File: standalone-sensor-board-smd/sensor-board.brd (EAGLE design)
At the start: 11 x 93.5 mm, 15 parts, among them Q1 QRE1113, Q2 QRE1113, Q3 QRE1113, Q4 QRE1113, Q5 QRE1113, Q6 QRE1113, Q7 QRE1113

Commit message: init smd
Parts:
- Q1, Q2, Q3, Q4, Q5, Q6, Q7: value QRE1113 -> QRE1113GR; device qre1113:DIP4_100AQ_ONS -> qre1113:DIP4_100AQ_ONS_SMD
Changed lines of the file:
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@@
 </autorouter>
 <elements>
-<element name="Q1" library="qre1113" package="DIP4_100AQ_ONS" value="QRE1113" x="1.705" y="3.71" smashed="yes">
+<element name="Q1" library="qre1113" package="DIP4_100AQ_ONS_SMD" value="QRE1113GR" x="1.705" y="3.71" smashed="yes">
 <attribute name="COPYRIGHT" value="Copyright (C) 2024 Ultra Librarian. All rights reserved." x="60.125" y="-8.99" size="1.778" layer="27" display="off"/>
 <attribute name="MANUFACTURER_PART_NUMBER" value="QRE1113" x="60.125" y="-8.99" size="1.778" layer="27" display="off"/>
@@
 <attribute name="NAME" x="4.336" y="3.4334" size="1.27" layer="27" ratio="6" rot="SR90"/>
 </element>
-<element name="Q2" library="qre1113" package="DIP4_100AQ_ONS" value="QRE1113" x="1.705" y="17.73" smashed="yes">
+<element name="Q2" library="qre1113" package="DIP4_100AQ_ONS_SMD" value="QRE1113GR" x="1.705" y="17.73" smashed="yes">
 <attribute name="COPYRIGHT" value="Copyright (C) 2024 Ultra Librarian. All rights reserved." x="29.645" y="-29.26" size="1.778" layer="27" display="off"/>
 <attribute name="MANUFACTURER_PART_NUMBER" value="QRE1113" x="29.645" y="-29.26" size="1.778" layer="27" display="off"/>
@@
 <attribute name="NAME" x="4.216" y="17.5334" size="1.27" layer="27" ratio="6" rot="SR90"/>
 </element>
-<element name="Q3" library="qre1113" package="DIP4_100AQ_ONS" value="QRE1113" x="1.705" y="31.75" smashed="yes">
+<element name="Q3" library="qre1113" package="DIP4_100AQ_ONS_SMD" value="QRE1113GR" x="1.705" y="31.75" smashed="yes">
 <attribute name="COPYRIGHT" value="Copyright (C) 2024 Ultra Librarian. All rights reserved." x="58.855" y="-15.24" size="1.778" layer="27" display="off"/>
 <attribute name="MANUFACTURER_PART_NUMBER" value="QRE1113" x="58.855" y="-15.24" size="1.778" layer="27" display="off"/>
@@
 <attribute name="NAME" x="4.196" y="31.5334" size="1.27" layer="27" ratio="6" rot="SR90"/>
 </element>
-<element name="Q4" library="qre1113" package="DIP4_100AQ_ONS" value="QRE1113" x="1.705" y="45.77" smashed="yes">
+<element name="Q4" library="qre1113" package="DIP4_100AQ_ONS_SMD" value="QRE1113GR" x="1.705" y="45.77" smashed="yes">
 <attribute name="COPYRIGHT" value="Copyright (C) 2024 Ultra Librarian. All rights reserved." x="29.645" y="-20.27" size="1.778" layer="27" display="off"/>
 <attribute name="MANUFACTURER_PART_NUMBER" value="QRE1113" x="29.645" y="-20.27" size="1.778" layer="27" display="off"/>
@@
 <attribute name="NAME" x="4.276" y="45.5334" size="1.27" layer="27" ratio="6" rot="SR90"/>
 </element>
-<element name="Q5" library="qre1113" package="DIP4_100AQ_ONS" value="QRE1113" x="1.705" y="59.79" smashed="yes">
+<element name="Q5" library="qre1113" package="DIP4_100AQ_ONS_SMD" value="QRE1113GR" x="1.705" y="59.79" smashed="yes">
 <attribute name="COPYRIGHT" value="Copyright (C) 2024 Ultra Librarian. All rights reserved." x="58.855" y="-6.25" size="1.778" layer="27" display="off"/>
 <attribute name="MANUFACTURER_PART_NUMBER" value="QRE1113" x="58.855" y="-6.25" size="1.778" layer="27" display="off"/>
@@
 <attribute name="NAME" x="4.256" y="59.5334" size="1.27" layer="27" ratio="6" rot="SR90"/>
 </element>
-<element name="Q6" library="qre1113" package="DIP4_100AQ_ONS" value="QRE1113" x="1.705" y="73.81" smashed="yes">
+<element name="Q6" library="qre1113" package="DIP4_100AQ_ONS_SMD" value="QRE1113GR" x="1.705" y="73.81" smashed="yes">
 <attribute name="COPYRIGHT" value="Copyright (C) 2024 Ultra Librarian. All rights reserved." x="29.645" y="-11.28" size="1.778" layer="27" display="off"/>
 <attribute name="MANUFACTURER_PART_NUMBER" value="QRE1113" x="29.645" y="-11.28" size="1.778" layer="27" display="off"/>
@@
 <attribute name="NAME" x="4.236" y="73.4334" size="1.27" layer="27" ratio="6" rot="SR90"/>
 </element>
-<element name="Q7" library="qre1113" package="DIP4_100AQ_ONS" value="QRE1113" x="1.705" y="87.83" smashed="yes">
+<element name="Q7" library="qre1113" package="DIP4_100AQ_ONS_SMD" value="QRE1113GR" x="1.705" y="87.83" smashed="yes">
 <attribute name="COPYRIGHT" value="Copyright (C) 2024 Ultra Librarian. All rights reserved." x="58.855" y="2.74" size="1.778" layer="27" display="off"/>
 <attribute name="MANUFACTURER_PART_NUMBER" value="QRE1113" x="58.855" y="2.74" size="1.778" layer="27" display="off"/>
@@
 <contactref element="Q1" pad="3"/>
 <contactref element="J1" pad="14"/>
-<wire x1="5.515" y1="5.5134" x2="5.4384375" y2="5.5134" width="0.1524" layer="16"/>
+<wire x1="5.515" y1="5.488" x2="5.4384375" y2="5.5134" width="0.1524" layer="16"/>
 <wire x1="5.4384375" y1="5.5134" x2="2.6958" y2="8.2560375" width="0.1524" layer="16"/>
 <wire x1="3.45" y1="40.25" x2="2.6958" y2="39.4958" width="0.1524" layer="16"/>
 <wire x1="2.6958" y1="39.4958" x2="2.6958" y2="8.2560375" width="0.1524" layer="16"/>
+<wire x1="5.515" y1="5.488" x2="5.515" y2="5.488" width="0" layer="19" extent="1-16"/>
 </signal>
 <signal name="GND">
@@
 <contactref element="J1" pad="MP1"/>
 <contactref element="J1" pad="MP2"/>
+<wire x1="1.705" y1="89.608" x2="5.515" y2="87.83" width="0" layer="19" extent="1-1"/>
+<wire x1="1.705" y1="75.588" x2="5.515" y2="87.83" width="0" layer="19" extent="1-1"/>
+<wire x1="5.515" y1="73.81" x2="1.705" y2="75.588" width="0" layer="19" extent="1-1"/>
+<wire x1="1.705" y1="61.568" x2="5.515" y2="73.81" width="0" layer="19" extent="1-1"/>
+<wire x1="5.515" y1="59.79" x2="1.705" y2="61.568" width="0" layer="19" extent="1-1"/>
+<wire x1="6.2" y1="55.55" x2="5.515" y2="59.79" width="0" layer="19" extent="1-16"/>
+<wire x1="3.45" y1="53.25" x2="6.2" y2="55.55" width="0" layer="19" extent="16-16"/>
+<wire x1="1.705" y1="47.548" x2="3.45" y2="53.25" width="0" layer="19" extent="1-16"/>
+<wire x1="5.515" y1="45.77" x2="1.705" y2="47.548" width="0" layer="19" extent="1-1"/>
+<wire x1="6.2" y1="37.95" x2="5.515" y2="45.77" width="0" layer="19" extent="1-16"/>
+<wire x1="5.515" y1="31.75" x2="6.2" y2="37.95" width="0" layer="19" extent="1-16"/>
+<wire x1="1.705" y1="33.528" x2="5.515" y2="31.75" width="0" layer="19" extent="1-1"/>
+<wire x1="1.705" y1="19.508" x2="5.515" y2="31.75" width="0" layer="19" extent="1-1"/>
+<wire x1="5.515" y1="17.73" x2="1.705" y2="19.508" width="0" layer="19" extent="1-1"/>
+<wire x1="1.705" y1="5.488" x2="5.515" y2="17.73" width="0" layer="19" extent="1-1"/>
+<wire x1="5.515" y1="3.71" x2="1.705" y2="5.488" width="0" layer="19" extent="1-1"/>
 </signal>
 <signal name="N$3">
@@
 <wire x1="4.1946875" y1="40.7786" x2="3.9214" y2="40.7786" width="0.1524" layer="16"/>
 <wire x1="3.9214" y1="40.7786" x2="3.45" y2="41.25" width="0.1524" layer="16"/>
-<wire x1="3.0006" y1="22.0478" x2="5.515" y2="19.5334" width="0.1524" layer="16"/>
+<wire x1="3.0006" y1="22.0478" x2="5.515" y2="19.508" width="0.1524" layer="16"/>
+<wire x1="5.515" y1="19.508" x2="5.515" y2="19.508" width="0" layer="19" extent="1-16"/>
 </signal>
 <signal name="N$5">
@@
 <wire x1="4.25" y1="42.25" x2="3.45" y2="42.25" width="0.1524" layer="16"/>
 <wire x1="7.4658" y1="39.0342" x2="4.25" y2="42.25" width="0.1524" layer="16"/>
-<wire x1="5.515" y1="33.5534" x2="7.4658" y2="35.5042" width="0.1524" layer="16"/>
+<wire x1="5.515" y1="33.528" x2="7.4658" y2="35.5042" width="0.1524" layer="16"/>
 <wire x1="7.4658" y1="35.5042" x2="7.4658" y2="39.0342" width="0.1524" layer="16"/>
+<wire x1="5.515" y1="33.528" x2="5.515" y2="33.528" width="0" layer="19" extent="1-16"/>
 </signal>
 <signal name="N$7">
@@
 <contactref element="Q4" pad="3"/>
 <contactref element="J1" pad="6"/>
-<wire x1="5.515" y1="47.5734" x2="5.0884" y2="48" width="0.1524" layer="16"/>
+<wire x1="5.515" y1="47.548" x2="5.0884" y2="48" width="0.1524" layer="16"/>
 <wire x1="3.7" y1="48" x2="3.45" y2="48.25" width="0.1524" layer="16"/>
 <wire x1="5.0884" y1="48" x2="3.7" y2="48" width="0.1524" layer="16"/>
+<wire x1="5.515" y1="47.548" x2="5.515" y2="47.548" width="0" layer="19" extent="1-16"/>
 </signal>
 <signal name="C4">
 <contactref element="Q5" pad="3"/>
 <contactref element="J1" pad="5"/>
-<wire x1="5.515" y1="61.5934" x2="8.011" y2="59.0974" width="0.1524" layer="16"/>
+<wire x1="5.515" y1="61.568" x2="8.011" y2="59.0974" width="0.1524" layer="16"/>
 <wire x1="8.011" y1="59.0974" x2="8.011" y2="58.8617625" width="0.1524" layer="16"/>
 <wire x1="9" y1="57.8727625" x2="9" y2="50.5" width="0.1524" layer="16"/>
@@
 <wire x1="9" y1="50.5" x2="7.75" y2="49.25" width="0.1524" layer="16"/>
 <wire x1="7.75" y1="49.25" x2="3.45" y2="49.25" width="0.1524" layer="16"/>
+<wire x1="5.515" y1="61.568" x2="5.515" y2="61.568" width="0" layer="19" extent="1-16"/>
 </signal>
 <signal name="N$11">
@@
 <contactref element="Q6" pad="3"/>
 <contactref element="J1" pad="4"/>
-<wire x1="5.515" y1="75.5" x2="5.515" y2="75.6134" width="0.1524" layer="16"/>
+<wire x1="5.515" y1="75.5" x2="5.515" y2="75.588" width="0.1524" layer="16"/>
 <wire x1="3.113428125" y1="58.886571875" x2="3" y2="58.77314375" width="0.1524" layer="16"/>
 <wire x1="3.113428125" y1="58.886571875" x2="3.113428125" y2="74.613428125" width="0.1524" layer="16"/>
@@
 <wire x1="3.2" y1="50.5" x2="3.45" y2="50.25" width="0.1524" layer="16"/>
 <wire x1="3" y1="58.77314375" x2="3" y2="58" width="0.1524" layer="16"/>
+<wire x1="5.515" y1="75.588" x2="5.515" y2="75.588" width="0" layer="19" extent="1-16"/>
 </signal>
 <signal name="N$13">
@@
 <wire x1="1.5" y1="51.5" x2="1.5" y2="57.7042" width="0.1524" layer="16"/>
 <wire x1="1.5" y1="57.7042" x2="2.7958" y2="59" width="0.1524" layer="16"/>
-<wire x1="2.7958" y1="86.9142" x2="5.515" y2="89.6334" width="0.1524" layer="16"/>
+<wire x1="2.7958" y1="86.9142" x2="5.515" y2="89.608" width="0.1524" layer="16"/>
 <wire x1="2.7958" y1="59" x2="2.7958" y2="86.9142" width="0.1524" layer="16"/>
+<wire x1="5.515" y1="89.608" x2="5.515" y2="89.608" width="0" layer="19" extent="1-16"/>
 </signal>
 <signal name="N$4">

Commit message: add smd boards from standalone
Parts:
- Q1, Q2, Q3, Q4, Q5, Q6, Q7: value QRE1113GR -> QRE1113; device qre1113:DIP4_100AQ_ONS_SMD -> qre1113:DIP4_100AQ_ONS
- R1, R11, R13, R3, R5, R7, R9: device rcl:0204V -> rcl:R0805
- moved R7 13.8 mm to (8.00, 46.5), flipped to the top, turned to 270 degrees
- moved R5 4.91 mm to (8.00, 32.5), turned to 270 degrees
- moved R3 3.01 mm to (8.00, 18.5), turned to 270 degrees
- moved R1 2.80 mm to (8.00, 4.50), turned to 270 degrees
- moved R13 2.77 mm to (8.00, 88.5), turned to 90 degrees
- moved R11 2.70 mm to (8.00, 74.5), turned to 270 degrees
- moved R9 0.90 mm to (8.00, 60.5)
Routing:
- net N$7: track 17.4 -> 6.96 mm
- net C6: track 41.8 -> 49.4 mm
- net N$4: track 13.5 -> 6.95 mm
- net C5: track 29.1 -> 35.5 mm, vias 2 -> 0
- net C4: track 18.6 -> 21.8 mm
- net N$13: track 5.69 -> 7.88 mm
- net N$3: track 5.65 -> 6.98 mm
- net N$1: track 5.86 -> 6.99 mm
- net N$11: track 5.86 -> 6.94 mm
- net C1: track 24.1 -> 23.3 mm
- net N$5: track 6.44 -> 6.97 mm

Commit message: clear out old boards
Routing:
- net C6: track 49.4 -> 47.3 mm
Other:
- board text removed: "NEMUS Sensor Board v0.2.0"

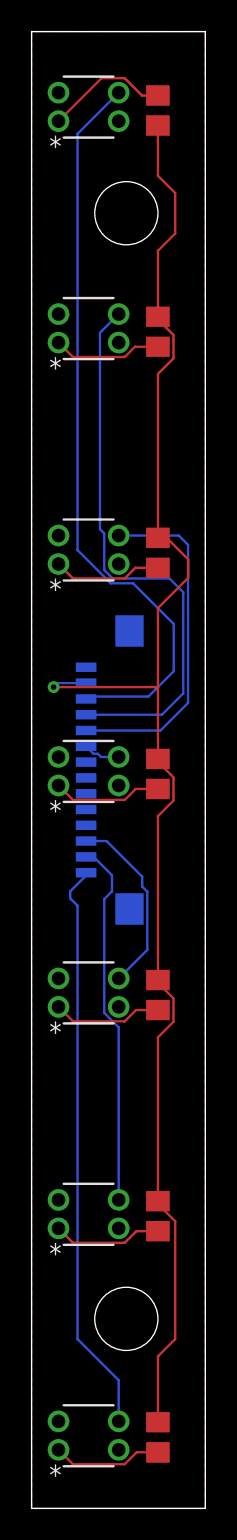
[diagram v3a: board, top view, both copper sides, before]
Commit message: tidy silk screen
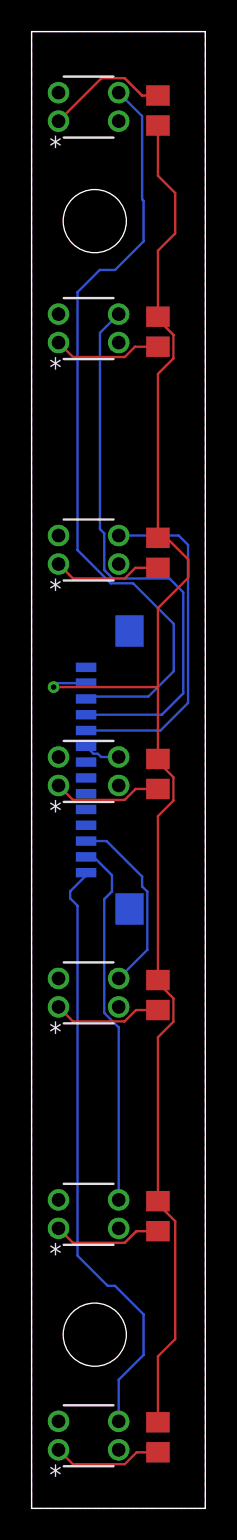
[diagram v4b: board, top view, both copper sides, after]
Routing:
- net C6: track 47.3 -> 49.2 mm
- net C0: track 36.4 -> 38.0 mm
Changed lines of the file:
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@@
 <layer number="97" name="Info" color="7" fill="1" visible="no" active="no"/>
 <layer number="98" name="Guide" color="6" fill="1" visible="no" active="no"/>
-<layer number="200" name="bBitMap" color="1" fill="10" visible="yes" active="yes"/>
+<layer number="200" name="bBmp" color="1" fill="10" visible="yes" active="yes"/>
 <layer number="250" name="Descript" color="7" fill="1" visible="yes" active="yes"/>
 <layer number="251" name="SMDround" color="7" fill="1" visible="yes" active="yes"/>
@@
 <rectangle x1="5.2" y1="68.58" x2="5.44" y2="68.62" layer="200" rot="R90"/>
 <rectangle x1="5.28" y1="69.54" x2="5.36" y2="69.58" layer="200" rot="R90"/>
-<hole x="6" y="12" drill="4"/>
-<hole x="6" y="82" drill="4"/>
+<hole x="4" y="11" drill="4"/>
+<hole x="4" y="81.5" drill="4"/>
 </plain>
 <attributes>
@@
 <contactref element="Q1" pad="3"/>
 <contactref element="J1" pad="14"/>
-<wire x1="5.515" y1="5.5134" x2="5.515" y2="8.11196875" width="0.1524" layer="16"/>
-<wire x1="5.515" y1="8.11196875" x2="2.9078" y2="10.71916875" width="0.1524" layer="16"/>
 <wire x1="2.44514375" y1="38.61945625" x2="2.44514375" y2="39.065528125" width="0.1524" layer="16"/>
 <wire x1="2.44514375" y1="39.065528125" x2="3.45" y2="40.070384375" width="0.1524" layer="16"/>
 <wire x1="3.45" y1="40.070384375" x2="3.45" y2="40.25" width="0.1524" layer="16"/>
 <wire x1="2.9078" y1="38.1568" x2="2.44514375" y2="38.61945625" width="0.1524" layer="16"/>
-<wire x1="2.9078" y1="10.71916875" x2="2.9078" y2="38.1568" width="0.1524" layer="16"/>
+<wire x1="2.9078" y1="16" x2="2.9078" y2="38.1568" width="0.1524" layer="16"/>
+<wire x1="5.515" y1="8.14196875" x2="7.0922" y2="9.71916875" width="0.1524" layer="16"/>
+<wire x1="7.0922" y1="9.71916875" x2="7.0922" y2="12.28083125" width="0.1524" layer="16"/>
+<wire x1="7.0922" y1="12.28083125" x2="5.28083125" y2="14.0922" width="0.1524" layer="16"/>
+<wire x1="5.28083125" y1="14.0922" x2="4.8156" y2="14.0922" width="0.1524" layer="16"/>
+<wire x1="4.8156" y1="14.0922" x2="2.9078" y2="16" width="0.1524" layer="16"/>
+<wire x1="5.515" y1="5.5134" x2="5.515" y2="8.14196875" width="0.1524" layer="16"/>
 </signal>
 <signal name="GND">
@@
 <wire x1="7.4" y1="51.4" x2="3.6" y2="51.4" width="0.1524" layer="16"/>
 <wire x1="6.4292" y1="58.5708" x2="9" y2="56" width="0.1524" layer="16"/>
-<wire x1="5.515" y1="89.6334" x2="2.9078" y2="87.0262" width="0.1524" layer="16"/>
-<wire x1="2.9078" y1="87.0262" x2="2.9078" y2="60.67298125" width="0.1524" layer="16"/>
+<wire x1="2.9078" y1="60.67298125" x2="2.9078" y2="77" width="0.1524" layer="16"/>
 <wire x1="2.9078" y1="60.67298125" x2="5.00998125" y2="58.5708" width="0.1524" layer="16"/>
+<wire x1="2.9078" y1="77" x2="4.3156" y2="78.4078" width="0.1524" layer="16"/>
+<wire x1="4.3156" y1="78.4078" x2="5.28083125" y2="78.4078" width="0.1524" layer="16"/>
+<wire x1="5.28083125" y1="78.4078" x2="7.0922" y2="80.21916875" width="0.1524" layer="16"/>
+<wire x1="7.0922" y1="80.21916875" x2="7.0922" y2="82.78083125" width="0.1524" layer="16"/>
+<wire x1="7.0922" y1="82.78083125" x2="7" y2="82.87303125" width="0.1524" layer="16"/>
+<wire x1="7" y1="88.1484" x2="5.515" y2="89.6334" width="0.1524" layer="16"/>
+<wire x1="7" y1="82.87303125" x2="7" y2="88.1484" width="0.1524" layer="16"/>
 </signal>
 <signal name="N$4">
